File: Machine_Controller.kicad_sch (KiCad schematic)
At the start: 34 parts, among them J1 SERIAL, J2 DEBUG, J3 LCD, SW1 SW_MEC_5E, SW2 RotaryEncoder_Switch, U1 STM32G050C8Tx, U2 AMS1117-3.3

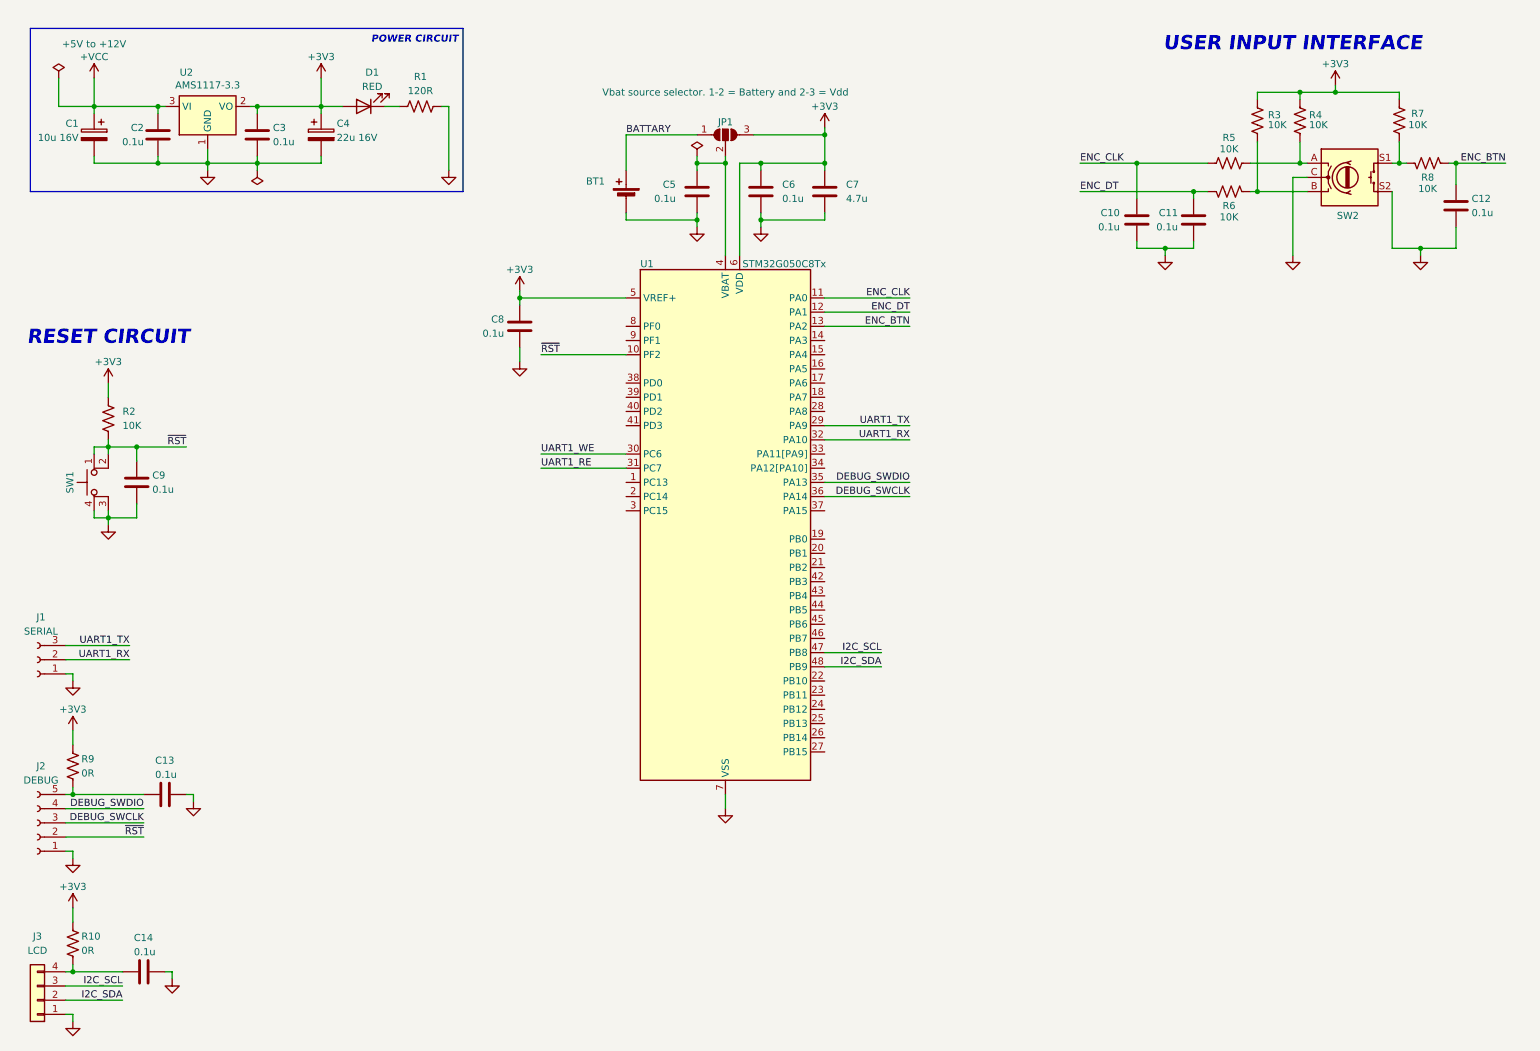
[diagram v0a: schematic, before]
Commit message: COM port and RS485 chip added
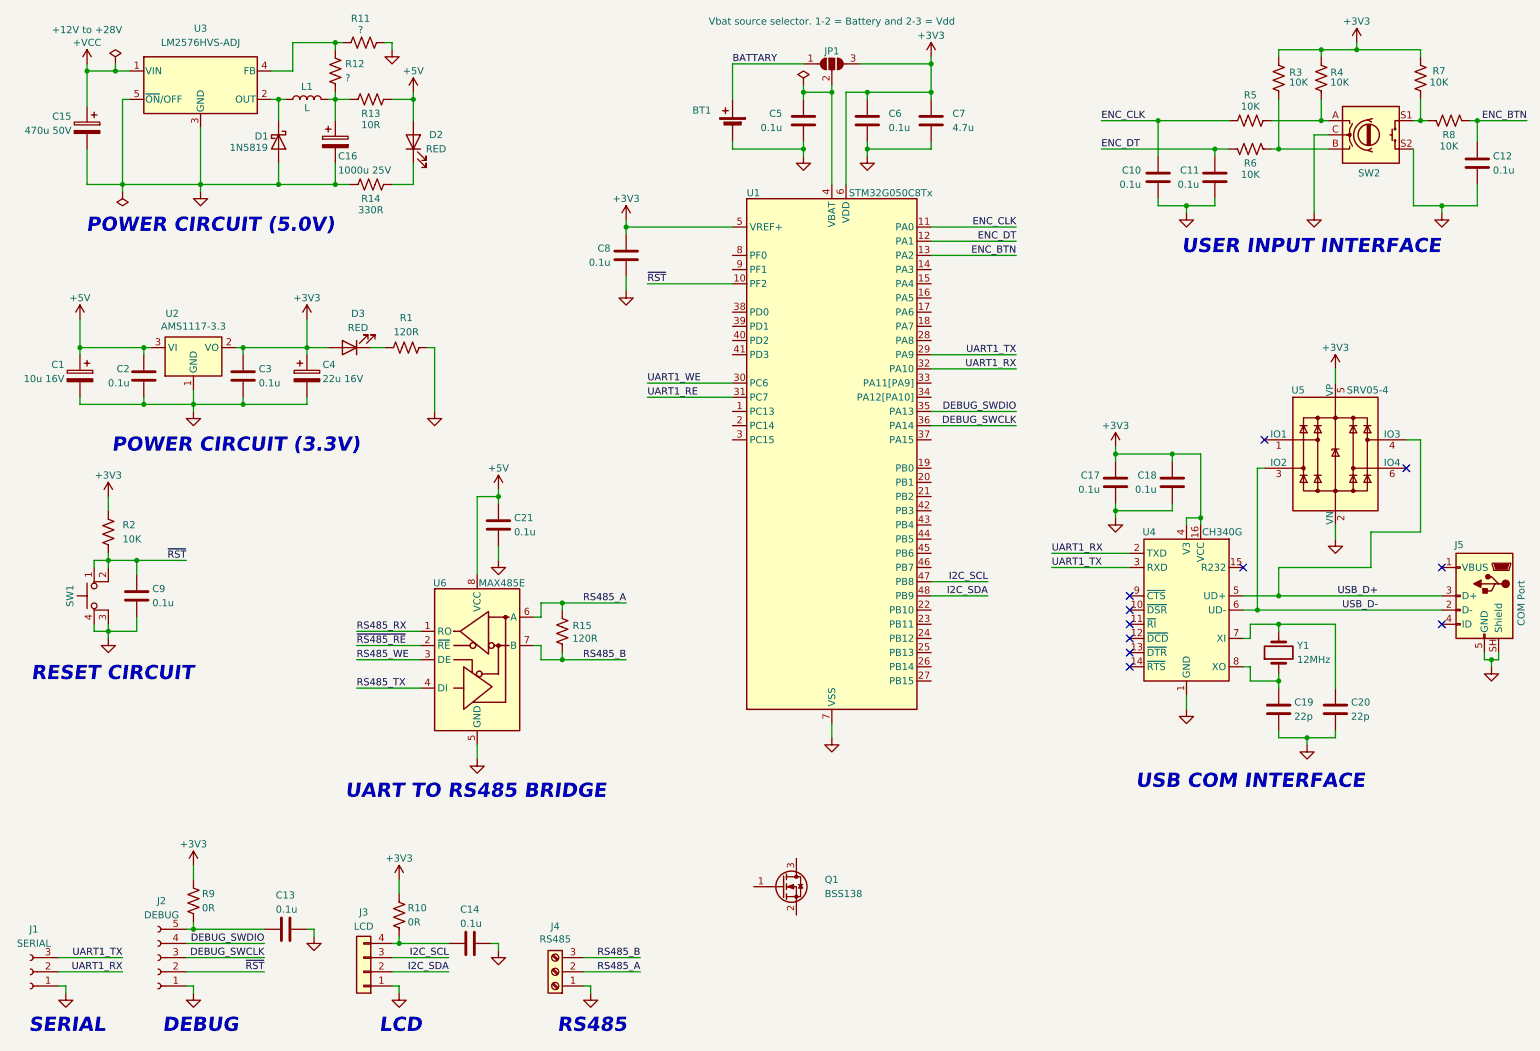
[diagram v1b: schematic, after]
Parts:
- added C15: 470u 50V, symbol Device:C_Polarized
- added C16: 1000u 25V, symbol Device:C_Polarized
- added C17, C18, C21: 0.1u, Capacitor_SMD:C_0603_1608Metric_Pad1.08x0.95mm_HandSolder, symbol Device:C
- added C19, C20: 22p, Capacitor_SMD:C_0603_1608Metric_Pad1.08x0.95mm_HandSolder, symbol Device:C
- added D1: 1N5819, Diode_THT:D_DO-41_SOD81_P10.16mm_Horizontal, symbol Diode:1N5819
- added D2: RED, LED_SMD:LED_0805_2012Metric_Pad1.15x1.40mm_HandSolder, symbol Device:LED
- added J4: RS485, symbol Connector:Screw_Terminal_01x03
- added J5: COM Port, Connector_USB:USB_Mini-B_Lumberg_2486_01_Horizontal, symbol Connector:USB_B_Mini
- added L1: L, symbol Device:L
- added Q1: BSS138, Package_TO_SOT_SMD:SOT-23, symbol Transistor_FET:BSS138
- added R11, R12: ?, Resistor_SMD:R_0805_2012Metric_Pad1.20x1.40mm_HandSolder, symbol Device:R_US
- added R13: 10R, Resistor_SMD:R_0805_2012Metric_Pad1.20x1.40mm_HandSolder, symbol Device:R_US
- added R14: 330R, Resistor_SMD:R_0805_2012Metric_Pad1.20x1.40mm_HandSolder, symbol Device:R_US
- added R15: 120R, Resistor_SMD:R_0805_2012Metric_Pad1.20x1.40mm_HandSolder, symbol Device:R_US
- added U3: LM2576HVS-ADJ, Package_TO_SOT_SMD:TO-263-5_TabPin3, symbol Regulator_Switching:LM2576HVS-ADJ
- added U4: CH340G, Package_SO:SOIC-16_3.9x9.9mm_P1.27mm, symbol Interface_USB:CH340G
- added U5: SRV05-4, Package_TO_SOT_SMD:SOT-23-6, symbol Power_Protection:SRV05-4
- added U6: MAX485E, Package_DIP:DIP-8_W7.62mm, symbol Interface_UART:MAX485E
- added Y1: 12MHz, symbol Device:Crystal
- renumbered D1 to D3
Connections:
- net +3V3: now also C17.1, C18.1, U4.16 (VCC), U4.4 (V3), U5.5 (VP)
- net +VCC: now also C15.1, U3.1 (VIN); no longer C1.1, C2.1, U2.3 (VI)
- net GND: now also C15.2, C16.2, C17.2, C18.2, C19.2, C20.2, C21.2, D1.2 (A), J4.1 (Pin_1), J5.5 (GND), J5.SH (Shield), R11.1, R14.1, U3.3 (GND), U3.5 (~{ON}/OFF), U4.1 (GND), U5.2 (VN), U6.5 (GND)
- net UART1_RX: now also U4.2 (TXD)
- net UART1_TX: now also U4.3 (RXD)
- new net: D2.1 (K), R14.2
- new net: R11.2, R12.1, U3.4 (FB)
- new net: C16.1, L1.2, R12.2, R13.1
- new net: C20.1, U4.7 (XI), Y1.2
- new net: D1.1 (K), L1.1, U3.2 (OUT)
- new net: C19.1, U4.8 (XO), Y1.1
- new net +5V: C1.1, C2.1, C21.1, D2.2 (A), R13.2, U2.3 (VI), U6.8 (VCC)
- new net RS485_A: J4.2 (Pin_2), R15.1, U6.6 (A)
- new net RS485_B: J4.3 (Pin_3), R15.2, U6.7 (B)
- new net RS485_RX: U6.1 (RO)
- new net RS485_TX: U6.4 (DI)
- new net RS485_WE: U6.3 (DE)
- new net USB_D+: J5.3 (D+), U4.5 (UD+), U5.4 (IO3)
- new net USB_D-: J5.2 (D-), U4.6 (UD-), U5.3 (IO2)
- new net ~{RS485_RE}: U6.2 (~{RE})
- no-connect marks 0 -> 11
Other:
- note added: "DEBUG"
- note added: "LCD"
- note added: "POWER CIRCUIT (3.3V)"
- note added: "POWER CIRCUIT (5.0V)"
- note added: "RS485"
- note added: "SERIAL"
- note added: "UART TO RS485 BRIDGE"
- note added: "USB COM INTERFACE"
- note removed: "POWER CIRCUIT"
- moved on the sheet: BT1, C1, C10, C11, C12, C13, C14, C2, C3, C4, C5, C6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

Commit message: Cloned into office PC
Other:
- title: (none) -> Machine Controller
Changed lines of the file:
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@@
 	(generator_version "10.0")
 	(paper "A4")
+	(title_block
+		(title "Machine Controller")
+		(date "2026-04-13")
+		(rev "V0.0")
+	)
 	(text "RS485"
 		(exclude_from_sim no)

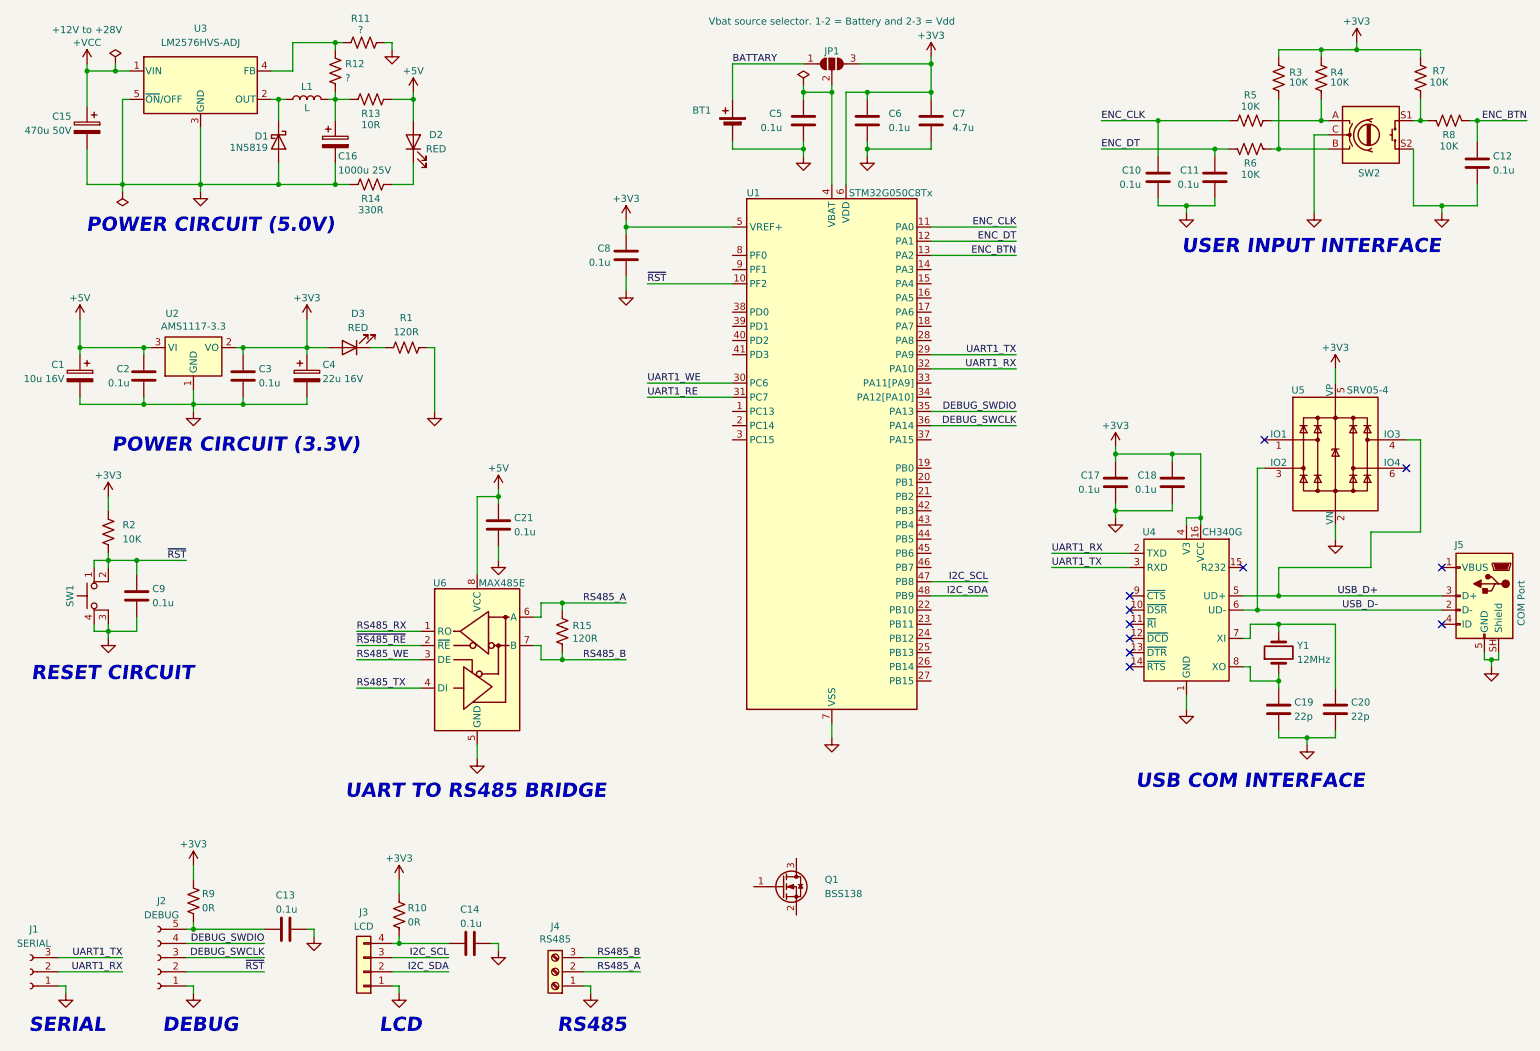
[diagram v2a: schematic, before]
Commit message: Input Output section added and modified
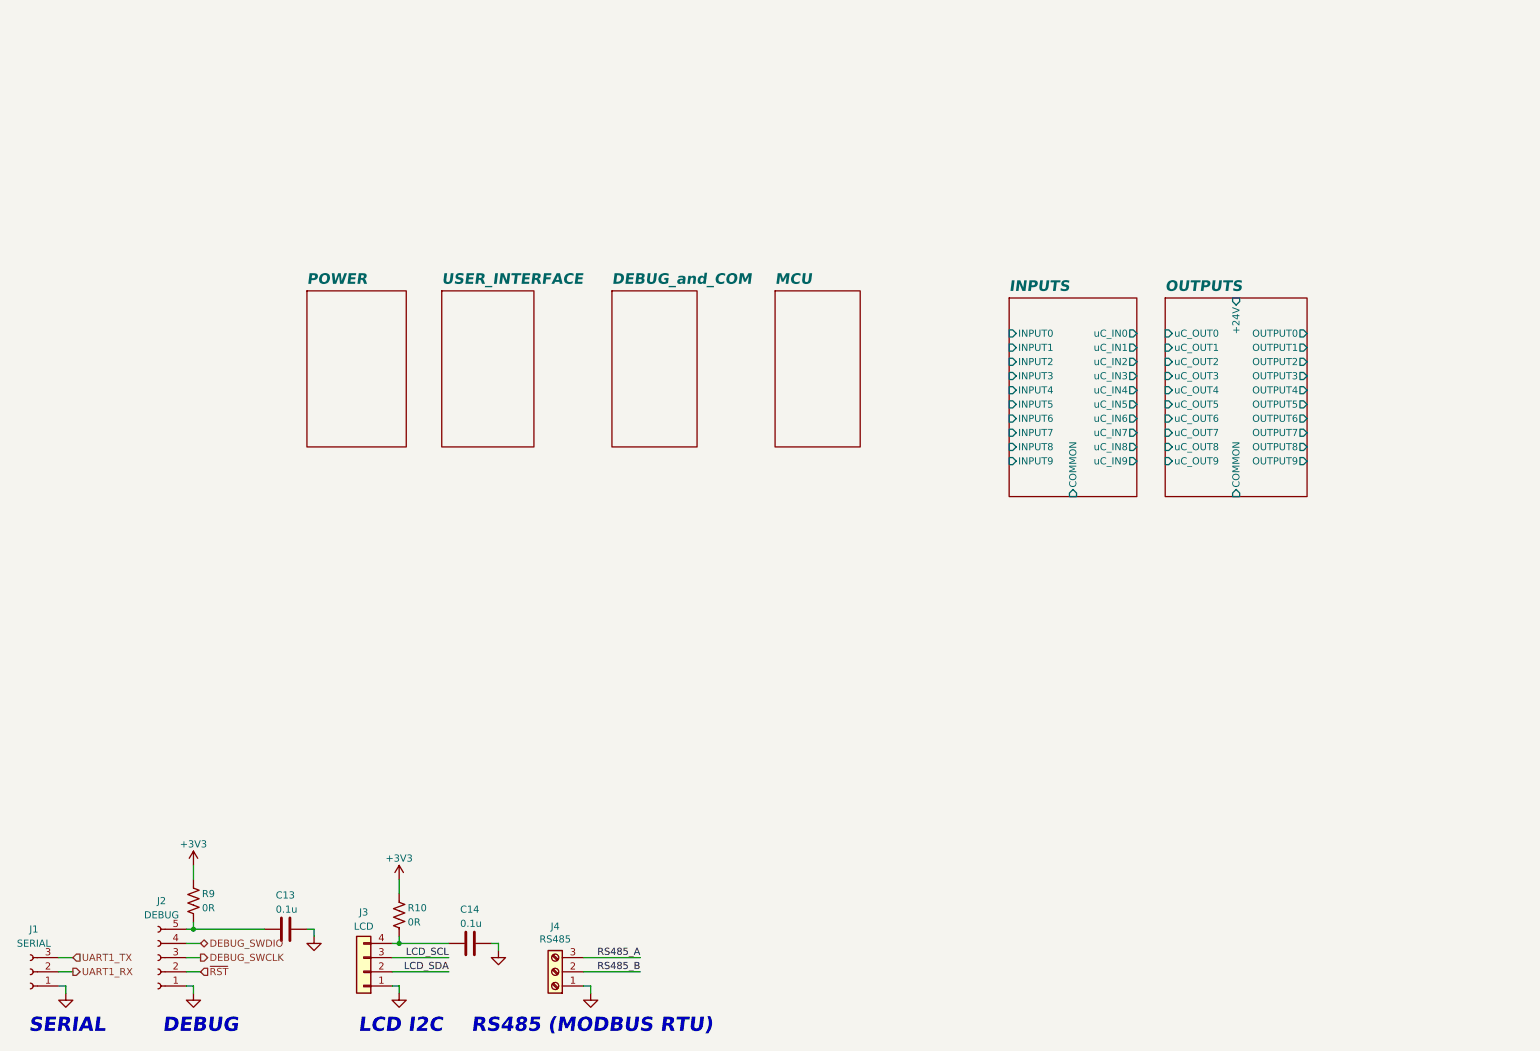
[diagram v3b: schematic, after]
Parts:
- removed BT1: CR2032, Battery:BatteryHolder_MYOUNG_BS-07-A1BJ001_CR2032, symbol Device:Battery_Cell
- removed C1: 10u 16V, symbol Device:C_Polarized
- removed C10, C11, C12, C17, C18, C2, C21, C3, C5, C6, C8, C9: 0.1u, Capacitor_SMD:C_0603_1608Metric_Pad1.08x0.95mm_HandSolder, symbol Device:C
- removed C15: 470u 50V, symbol Device:C_Polarized
- removed C16: 1000u 25V, symbol Device:C_Polarized
- removed C19, C20: 22p, Capacitor_SMD:C_0603_1608Metric_Pad1.08x0.95mm_HandSolder, symbol Device:C
- removed C4: 22u 16V, symbol Device:C_Polarized
- removed C7: 4.7u, Capacitor_SMD:C_0603_1608Metric_Pad1.08x0.95mm_HandSolder, symbol Device:C
- removed D1: 1N5819, Diode_THT:D_DO-41_SOD81_P10.16mm_Horizontal, symbol Diode:1N5819
- removed D2, D3: RED, LED_SMD:LED_0805_2012Metric_Pad1.15x1.40mm_HandSolder, symbol Device:LED
- removed J5: COM Port, Connector_USB:USB_Mini-B_Lumberg_2486_01_Horizontal, symbol Connector:USB_B_Mini
- removed JP1: SolderJumper_3_Open, Jumper:SolderJumper-3_P1.3mm_Open_Pad1.0x1.5mm, symbol Jumper:SolderJumper_3_Open
- removed L1: L, symbol Device:L
- removed Q1: BSS138, Package_TO_SOT_SMD:SOT-23, symbol Transistor_FET:BSS138
- removed R1, R15: 120R, Resistor_SMD:R_0805_2012Metric_Pad1.20x1.40mm_HandSolder, symbol Device:R_US
- removed R11, R12: ?, Resistor_SMD:R_0805_2012Metric_Pad1.20x1.40mm_HandSolder, symbol Device:R_US
- removed R13: 10R, Resistor_SMD:R_0805_2012Metric_Pad1.20x1.40mm_HandSolder, symbol Device:R_US
- removed R14: 330R, Resistor_SMD:R_0805_2012Metric_Pad1.20x1.40mm_HandSolder, symbol Device:R_US
- removed R2, R3, R4, R5, R6, R7, R8: 10K, Resistor_SMD:R_0805_2012Metric_Pad1.20x1.40mm_HandSolder, symbol Device:R_US
- removed SW1: SW_MEC_5E, symbol Switch:SW_MEC_5E
- removed SW2: RotaryEncoder_Switch, Rotary_Encoder:RotaryEncoder_Alps_EC11E-Switch_Vertical_H20mm, symbol Device:RotaryEncoder_Switch
- removed U1: STM32G050C8Tx, Package_QFP:LQFP-48_7x7mm_P0.5mm, symbol MCU_ST_STM32G0_LQFP48:STM32G050C8Tx
- removed U2: AMS1117-3.3, Package_TO_SOT_SMD:SOT-223-3_TabPin2, symbol Regulator_Linear:AMS1117-3.3
- removed U3: LM2576HVS-ADJ, Package_TO_SOT_SMD:TO-263-5_TabPin3, symbol Regulator_Switching:LM2576HVS-ADJ
- removed U4: CH340G, Package_SO:SOIC-16_3.9x9.9mm_P1.27mm, symbol Interface_USB:CH340G
- removed U5: SRV05-4, Package_TO_SOT_SMD:SOT-23-6, symbol Power_Protection:SRV05-4
- removed U6: MAX485E, Package_DIP:DIP-8_W7.62mm, symbol Interface_UART:MAX485E
- removed Y1: 12MHz, symbol Device:Crystal
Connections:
- net RS485_A: now also J4.3 (Pin_3); no longer J4.2 (Pin_2)
- net RS485_B: now also J4.2 (Pin_2); no longer J4.3 (Pin_3)
- net I2C_SCL renamed LCD_SCL
- net I2C_SDA renamed LCD_SDA
- no-connect marks 11 -> 0
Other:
- added sheet DEBUG_and_COM (DEBUG_and_COM.kicad_sch)
- added sheet INPUTS (INPUTS.kicad_sch)
- added sheet MCU (MCU.kicad_sch)
- added sheet OUTPUTS (OUTPUTS.kicad_sch)
- added sheet POWER (POWER.kicad_sch)
- added sheet USER_INTERFACE (USER_INTERFACE.kicad_sch)
- note added: "LCD I2C"
- note added: "RS485 (MODBUS RTU)"
- note removed: "LCD"
- note removed: "POWER CIRCUIT (3.3V)"
- note removed: "POWER CIRCUIT (5.0V)"
- note removed: "RESET CIRCUIT"
- note removed: "RS485"
- note removed: "UART TO RS485 BRIDGE"
- note removed: "USB COM INTERFACE"
- note removed: "USER INPUT INTERFACE"
